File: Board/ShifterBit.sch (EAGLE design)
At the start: 13 parts, among them P1 PINHD-1X10, P2 PINHD-1X10

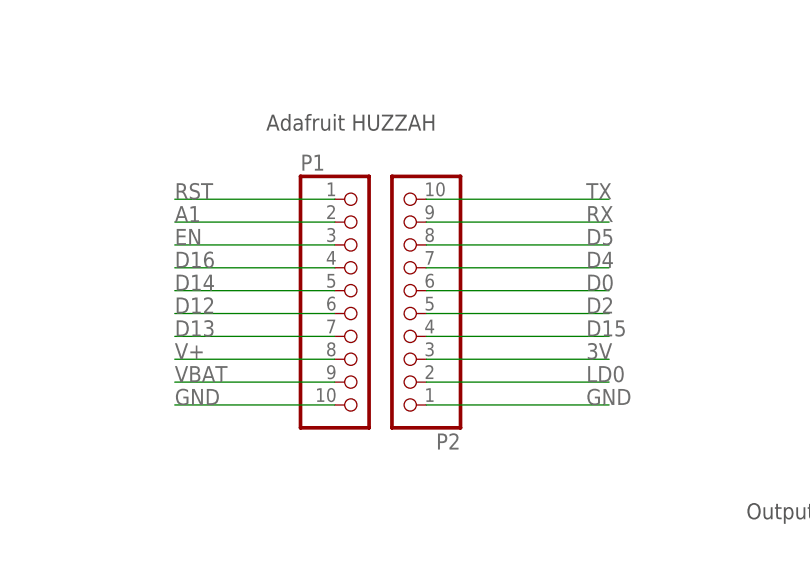
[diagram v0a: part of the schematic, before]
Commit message: removed unused nets
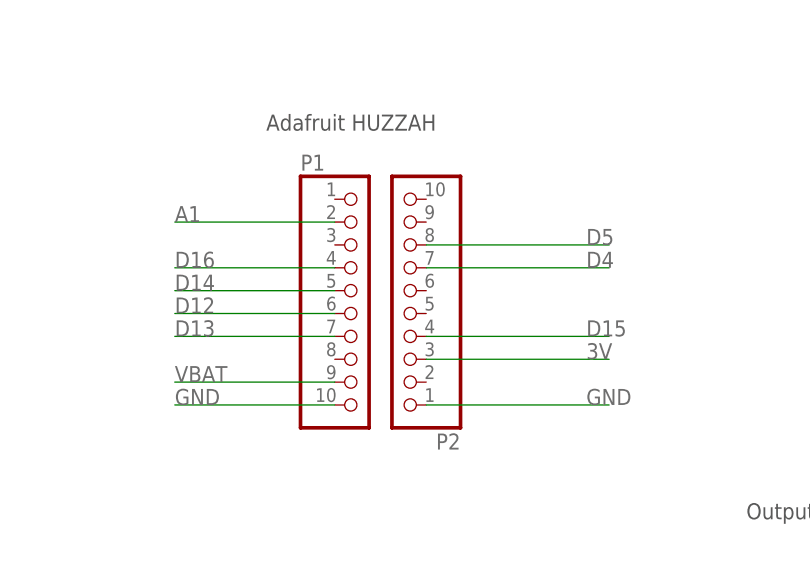
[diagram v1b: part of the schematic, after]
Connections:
- removed net D0: P2.6
- removed net D2: P2.5
- removed net EN: P1.3
- removed net LD0: P2.2
- removed net RST: P1.1
- removed net RX: P2.9
- removed net TX: P2.10
- removed net V+: P1.8
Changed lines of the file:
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@@
-</segment>
-</net>
-<net name="RST" class="0">
-<segment>
-<pinref part="P1" gate="G$1" pin="1"/>
-<wire x1="137.16" y1="142.24" x2="119.38" y2="142.24" width="0.1524" layer="91"/>
-<label x="119.38" y="142.24" size="1.778" layer="95"/>
 </segment>
 </net>
@@
 <junction x="60.96" y="144.78"/>
 <label x="76.2" y="144.78" size="1.778" layer="95"/>
-</segment>
-</net>
-<net name="EN" class="0">
-<segment>
-<pinref part="P1" gate="G$1" pin="3"/>
-<wire x1="137.16" y1="137.16" x2="119.38" y2="137.16" width="0.1524" layer="91"/>
-<label x="119.38" y="137.16" size="1.778" layer="95"/>
 </segment>
 </net>
@@
 </segment>
 </net>
-<net name="V+" class="0">
-<segment>
-<pinref part="P1" gate="G$1" pin="8"/>
-<wire x1="137.16" y1="124.46" x2="119.38" y2="124.46" width="0.1524" layer="91"/>
-<label x="119.38" y="124.46" size="1.778" layer="95"/>
-</segment>
-</net>
 <net name="VBAT" class="0">
 <segment>
@@
 <wire x1="137.16" y1="121.92" x2="119.38" y2="121.92" width="0.1524" layer="91"/>
 <label x="119.38" y="121.92" size="1.778" layer="95"/>
-</segment>
-</net>
-<net name="TX" class="0">
-<segment>
-<pinref part="P2" gate="G$1" pin="10"/>
-<wire x1="147.32" y1="142.24" x2="167.64" y2="142.24" width="0.1524" layer="91"/>
-<label x="165.1" y="142.24" size="1.778" layer="95"/>
-</segment>
-</net>
-<net name="RX" class="0">
-<segment>
-<pinref part="P2" gate="G$1" pin="9"/>
-<wire x1="147.32" y1="139.7" x2="167.64" y2="139.7" width="0.1524" layer="91"/>
-<label x="165.1" y="139.7" size="1.778" layer="95"/>
 </segment>
 </net>
@@
 </segment>
 </net>
-<net name="D0" class="0">
-<segment>
-<pinref part="P2" gate="G$1" pin="6"/>
-<wire x1="147.32" y1="132.08" x2="167.64" y2="132.08" width="0.1524" layer="91"/>
-<label x="165.1" y="132.08" size="1.778" layer="95"/>
-</segment>
-</net>
-<net name="D2" class="0">
-<segment>
-<pinref part="P2" gate="G$1" pin="5"/>
-<wire x1="147.32" y1="129.54" x2="167.64" y2="129.54" width="0.1524" layer="91"/>
-<label x="165.1" y="129.54" size="1.778" layer="95"/>
-</segment>
-</net>
 <net name="D15" class="0">
 <segment>
@@
 </segment>
 </net>
-<net name="LD0" class="0">
-<segment>
-<pinref part="P2" gate="G$1" pin="2"/>
-<wire x1="147.32" y1="121.92" x2="167.64" y2="121.92" width="0.1524" layer="91"/>
-<label x="165.1" y="121.92" size="1.778" layer="95"/>
-</segment>
-</net>

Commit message: grounded cd
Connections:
- net GND: now also SD1.CD
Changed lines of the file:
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@@
 <label x="223.52" y="132.08" size="1.778" layer="95"/>
+</segment>
+<segment>
+<pinref part="SD1" gate="A" pin="CD"/>
+<wire x1="144.78" y1="40.64" x2="160.02" y2="40.64" width="0.1524" layer="91"/>
+<label x="157.48" y="40.64" size="1.778" layer="95"/>
 </segment>
 </net>

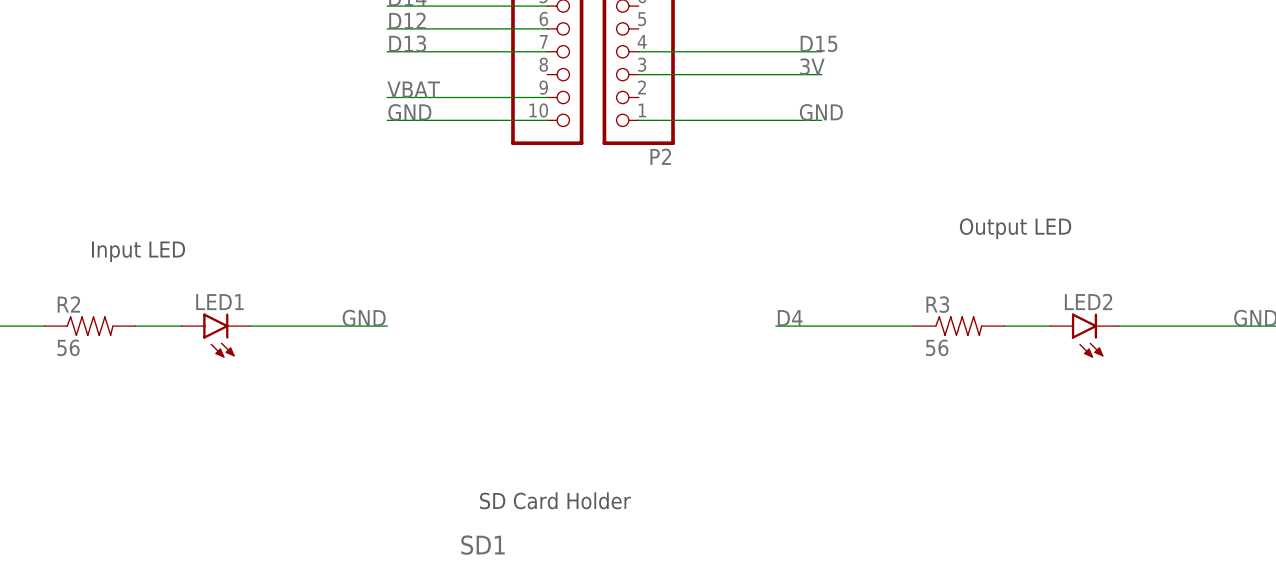
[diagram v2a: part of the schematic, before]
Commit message: use 1206 packages
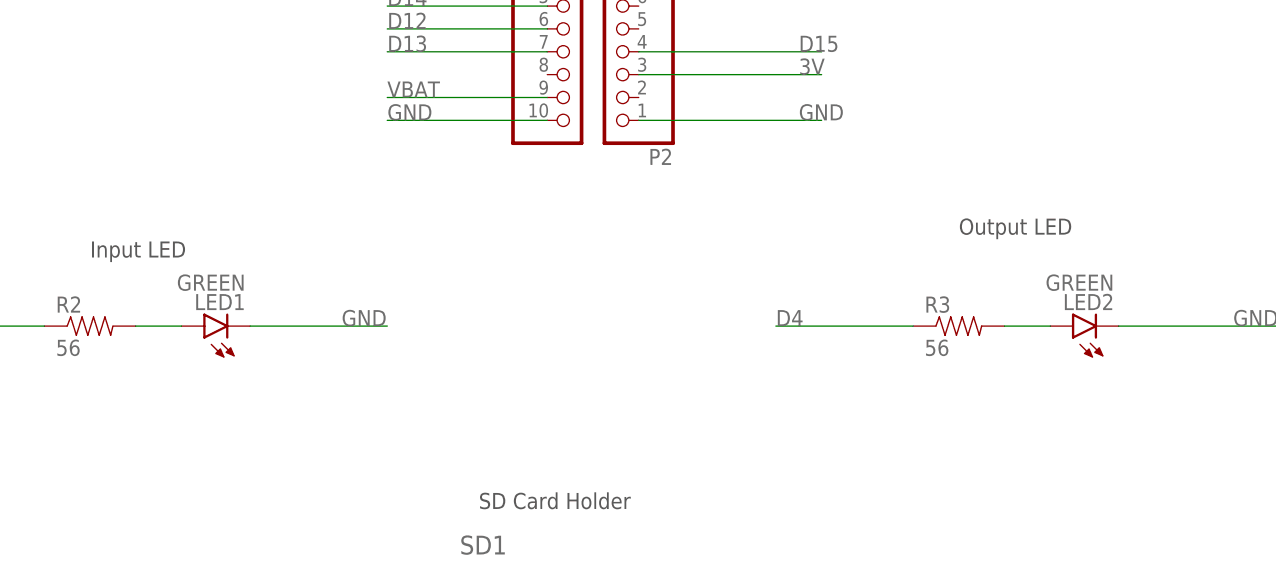
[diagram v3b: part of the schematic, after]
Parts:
- LED1, LED2: value (none) -> GREEN; device SparkFun-LED:LED-GREEN0603 -> SparkFun-LED:LED-GREENLARGE
- R1: device LITTLEBITS:RESISTOR0603 -> LITTLEBITS:RESISTOR1206
- R2, R3, R4, R5: device SparkFun-Passives:RESISTOR0603-RES -> SparkFun-Passives:RESISTOR1206

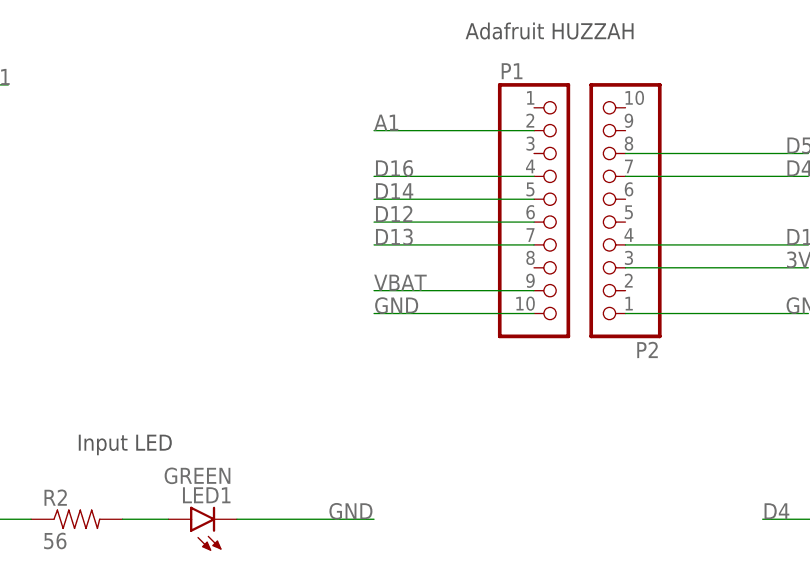
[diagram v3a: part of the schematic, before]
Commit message: fixed missing connection
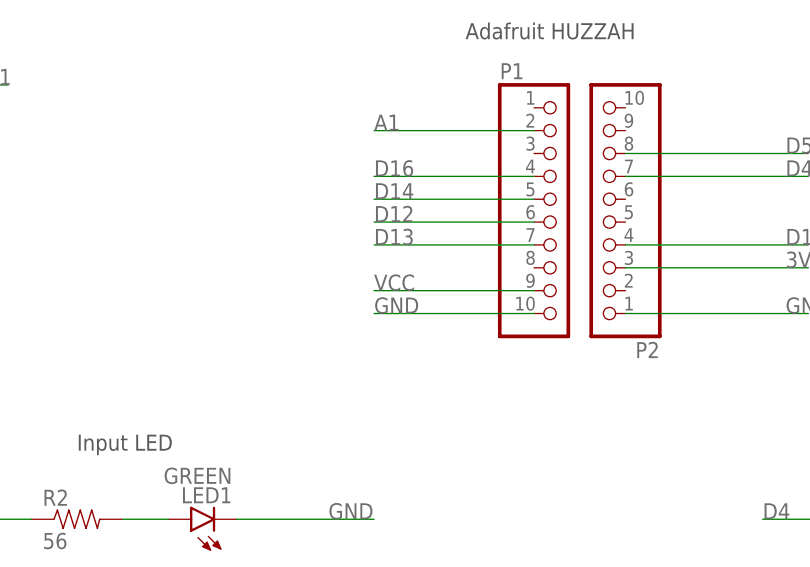
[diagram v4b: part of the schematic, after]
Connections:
- removed net VBAT: P1.9
- net VCC: now also P1.9
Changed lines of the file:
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@@
 <grid distance="0.1" unitdist="inch" unit="inch" style="lines" multiple="1" display="no" altdistance="0.01" altunitdist="inch" altunit="inch"/>
 <layers>
-<layer number="1" name="Top" color="4" fill="1" visible="yes" active="no"/>
-<layer number="2" name="Route2" color="1" fill="3" visible="yes" active="no"/>
-<layer number="3" name="Route3" color="4" fill="3" visible="yes" active="no"/>
-<layer number="4" name="Route4" color="1" fill="4" visible="yes" active="no"/>
-<layer number="5" name="Route5" color="4" fill="4" visible="yes" active="no"/>
-<layer number="6" name="Route6" color="1" fill="8" visible="yes" active="no"/>
-<layer number="7" name="Route7" color="4" fill="8" visible="yes" active="no"/>
-<layer number="8" name="Route8" color="1" fill="2" visible="yes" active="no"/>
-<layer number="9" name="Route9" color="4" fill="2" visible="yes" active="no"/>
-<layer number="10" name="Route10" color="1" fill="7" visible="yes" active="no"/>
-<layer number="11" name="Route11" color="4" fill="7" visible="yes" active="no"/>
-<layer number="12" name="Route12" color="1" fill="5" visible="yes" active="no"/>
-<layer number="13" name="Route13" color="4" fill="5" visible="yes" active="no"/>
-<layer number="14" name="Route14" color="1" fill="6" visible="yes" active="no"/>
-<layer number="15" name="Route15" color="4" fill="6" visible="yes" active="no"/>
-<layer number="16" name="Bottom" color="1" fill="1" visible="yes" active="no"/>
-<layer number="17" name="Pads" color="2" fill="1" visible="yes" active="no"/>
-<layer number="18" name="Vias" color="2" fill="1" visible="yes" active="no"/>
-<layer number="19" name="Unrouted" color="6" fill="1" visible="yes" active="no"/>
-<layer number="20" name="Dimension" color="15" fill="1" visible="yes" active="no"/>
-<layer number="21" name="tPlace" color="16" fill="1" visible="yes" active="no"/>
-<layer number="22" name="bPlace" color="14" fill="1" visible="yes" active="no"/>
-<layer number="23" name="tOrigins" color="15" fill="1" visible="yes" active="no"/>
-<layer number="24" name="bOrigins" color="15" fill="1" visible="yes" active="no"/>
-<layer number="25" name="tNames" color="7" fill="1" visible="yes" active="no"/>
-<layer number="26" name="bNames" color="7" fill="1" visible="yes" active="no"/>
-<layer number="27" name="tValues" color="7" fill="1" visible="yes" active="no"/>
-<layer number="28" name="bValues" color="7" fill="1" visible="yes" active="no"/>
+<layer number="1" name="Top" color="4" fill="1" visible="no" active="no"/>
+<layer number="2" name="Route2" color="1" fill="3" visible="no" active="no"/>
+<layer number="3" name="Route3" color="4" fill="3" visible="no" active="no"/>
+<layer number="4" name="Route4" color="1" fill="4" visible="no" active="no"/>
+<layer number="5" name="Route5" color="4" fill="4" visible="no" active="no"/>
+<layer number="6" name="Route6" color="1" fill="8" visible="no" active="no"/>
+<layer number="7" name="Route7" color="4" fill="8" visible="no" active="no"/>
+<layer number="8" name="Route8" color="1" fill="2" visible="no" active="no"/>
+<layer number="9" name="Route9" color="4" fill="2" visible="no" active="no"/>
+<layer number="10" name="Route10" color="1" fill="7" visible="no" active="no"/>
+<layer number="11" name="Route11" color="4" fill="7" visible="no" active="no"/>
+<layer number="12" name="Route12" color="1" fill="5" visible="no" active="no"/>
+<layer number="13" name="Route13" color="4" fill="5" visible="no" active="no"/>
+<layer number="14" name="Route14" color="1" fill="6" visible="no" active="no"/>
+<layer number="15" name="Route15" color="4" fill="6" visible="no" active="no"/>
+<layer number="16" name="Bottom" color="1" fill="1" visible="no" active="no"/>
+<layer number="17" name="Pads" color="2" fill="1" visible="no" active="no"/>
+<layer number="18" name="Vias" color="2" fill="1" visible="no" active="no"/>
+<layer number="19" name="Unrouted" color="6" fill="1" visible="no" active="no"/>
+<layer number="20" name="Dimension" color="15" fill="1" visible="no" active="no"/>
+<layer number="21" name="tPlace" color="16" fill="1" visible="no" active="no"/>
+<layer number="22" name="bPlace" color="14" fill="1" visible="no" active="no"/>
+<layer number="23" name="tOrigins" color="15" fill="1" visible="no" active="no"/>
+<layer number="24" name="bOrigins" color="15" fill="1" visible="no" active="no"/>
+<layer number="25" name="tNames" color="7" fill="1" visible="no" active="no"/>
+<layer number="26" name="bNames" color="7" fill="1" visible="no" active="no"/>
+<layer number="27" name="tValues" color="7" fill="1" visible="no" active="no"/>
+<layer number="28" name="bValues" color="7" fill="1" visible="no" active="no"/>
 <layer number="29" name="tStop" color="7" fill="3" visible="no" active="no"/>
 <layer number="30" name="bStop" color="7" fill="6" visible="no" active="no"/>
@@
 <layer number="35" name="tGlue" color="7" fill="4" visible="no" active="no"/>
 <layer number="36" name="bGlue" color="7" fill="5" visible="no" active="no"/>
-<layer number="37" name="tTest" color="7" fill="1" visible="yes" active="no"/>
-<layer number="38" name="bTest" color="7" fill="1" visible="yes" active="no"/>
+<layer number="37" name="tTest" color="7" fill="1" visible="no" active="no"/>
+<layer number="38" name="bTest" color="7" fill="1" visible="no" active="no"/>
 <layer number="39" name="tKeepout" color="4" fill="11" visible="no" active="no"/>
 <layer number="40" name="bKeepout" color="1" fill="11" visible="no" active="no"/>
@@
 <layer number="44" name="Drills" color="7" fill="1" visible="no" active="no"/>
 <layer number="45" name="Holes" color="7" fill="1" visible="no" active="no"/>
-<layer number="46" name="Milling" color="3" fill="1" visible="yes" active="no"/>
-<layer number="47" name="Measures" color="7" fill="1" visible="yes" active="no"/>
-<layer number="48" name="Document" color="7" fill="1" visible="yes" active="no"/>
-<layer number="49" name="Reference" color="10" fill="1" visible="yes" active="no"/>
-<layer number="50" name="dxf" color="7" fill="1" visible="yes" active="no"/>
-<layer number="51" name="tDocu" color="6" fill="1" visible="yes" active="no"/>
-<layer number="52" name="bDocu" color="7" fill="1" visible="yes" active="no"/>
-<layer number="53" name="tGND_GNDA" color="7" fill="9" visible="yes" active="no"/>
-<layer number="54" name="bGND_GNDA" color="1" fill="9" visible="yes" active="no"/>
-<layer number="56" name="wert" color="7" fill="1" visible="yes" active="no"/>
-<layer number="57" name="tCAD" color="7" fill="1" visible="yes" active="no"/>
-<layer number="59" name="tCarbon" color="7" fill="1" visible="yes" active="no"/>
-<layer number="60" name="bCarbon" color="7" fill="1" visible="yes" active="no"/>
+<layer number="46" name="Milling" color="3" fill="1" visible="no" active="no"/>
+<layer number="47" name="Measures" color="7" fill="1" visible="no" active="no"/>
+<layer number="48" name="Document" color="7" fill="1" visible="no" active="no"/>
+<layer number="49" name="Reference" color="10" fill="1" visible="no" active="no"/>
+<layer number="50" name="dxf" color="7" fill="1" visible="no" active="no"/>
+<layer number="51" name="tDocu" color="6" fill="1" visible="no" active="no"/>
+<layer number="52" name="bDocu" color="7" fill="1" visible="no" active="no"/>
+<layer number="53" name="tGND_GNDA" color="7" fill="9" visible="no" active="no"/>
+<layer number="54" name="bGND_GNDA" color="1" fill="9" visible="no" active="no"/>
+<layer number="56" name="wert" color="7" fill="1" visible="no" active="no"/>
+<layer number="57" name="tCAD" color="7" fill="1" visible="no" active="no"/>
+<layer number="59" name="tCarbon" color="7" fill="1" visible="no" active="no"/>
+<layer number="60" name="bCarbon" color="7" fill="1" visible="no" active="no"/>
 <layer number="90" name="Modules" color="5" fill="1" visible="yes" active="yes"/>
 <layer number="91" name="Nets" color="2" fill="1" visible="yes" active="yes"/>
@@
 <label x="223.52" y="152.4" size="1.778" layer="95"/>
 </segment>
+<segment>
+<pinref part="P1" gate="G$1" pin="9"/>
+<wire x1="137.16" y1="121.92" x2="119.38" y2="121.92" width="0.1524" layer="91"/>
+<label x="119.38" y="121.92" size="1.778" layer="95"/>
+</segment>
 </net>
 <net name="SIG_OUT" class="0">
@@
 </segment>
 </net>
-<net name="VBAT" class="0">
-<segment>
-<pinref part="P1" gate="G$1" pin="9"/>
-<wire x1="137.16" y1="121.92" x2="119.38" y2="121.92" width="0.1524" layer="91"/>
-<label x="119.38" y="121.92" size="1.778" layer="95"/>
-</segment>
-</net>
